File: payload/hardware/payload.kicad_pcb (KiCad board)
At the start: 4 copper layers, 80 x 80 mm, 43 parts, among them J10 Conn_02x20_Odd_Even, J2 ARJM11C7-502-AB, J3 USB_C_Receptacle_USB2.0_16P, J4 Conn_02x04_Odd_Even, J5 Conn_01x05, SW1 SW_Push, U1 CM4, U2 MCP2517FD-xJHA, U4 SN65HVD230, U5 MCP2517FD-xJHA, U6 74LVC1G07, U7 SN65HVD230, U9 DRV8846, Y1 20 MHz, Y2 20 MHz

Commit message: via spam, silk
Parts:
- added REF**: OSHW-Logo2_14.6x12mm_SilkScreen, Symbol:OSHW-Logo2_14.6x12mm_SilkScreen, B.Cu at (87.1, 129.1)
- SW1: footprint Button_Switch_SMD:SW_SPST_TS-1088-xR020 -> Button_Switch_SMD:SW_SPST_PTS810
- moved SW1 0.60 mm to (76.4, 82.2)
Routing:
- net /CM4/POWER_BUTTON: track 15.8 -> 21.4 mm
- net Net-(JP1-B): track 4.44 -> 7.82 mm
- net +5V: track 34.9 -> 31.6 mm, vias 1 -> 3
- net /CM4/ETH_P0-: track 28.5 -> 31.1 mm
- net /CM4/ETH_P2-: track 28.0 -> 30.5 mm
- net /CM4/ETH_P1+: track 25.9 -> 28.5 mm
- net /CM4/ETH_P3-: track 26.3 -> 27.9 mm
- net /CM4/Cameras/CAMERA_GPIO: track 102.4 -> 100.9 mm
- net /CM4/~{MOTOR_SLEEP}: track 61.1 -> 62.1 mm
- net Net-(J4-Pin_2): track 38.4 -> 39.1 mm
- net GND: vias 227 -> 536
- net +3V3: vias 15 -> 18
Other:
- board text added: "Ethan Eggbert frrt.space"
- board text added: "foo"

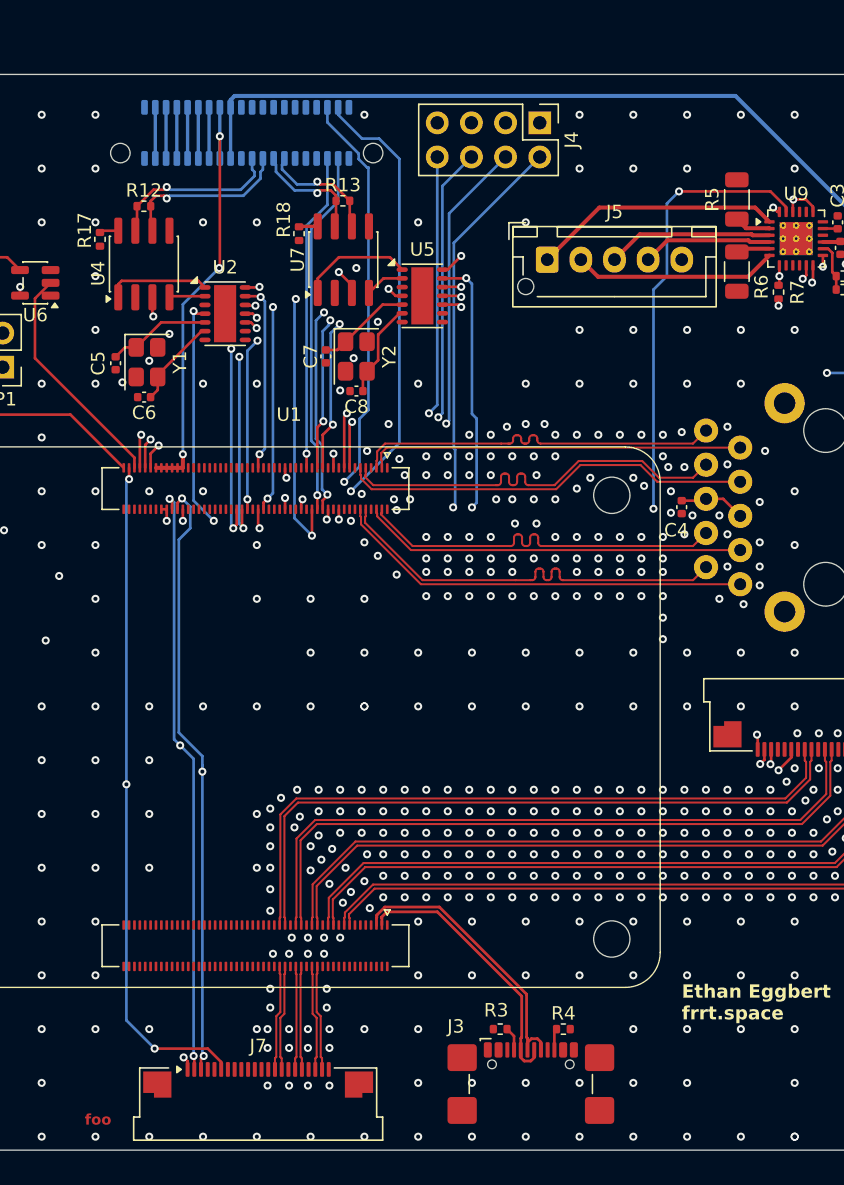
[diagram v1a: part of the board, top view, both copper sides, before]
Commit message: add decoupling caps, fix USB skew, add Jax's name
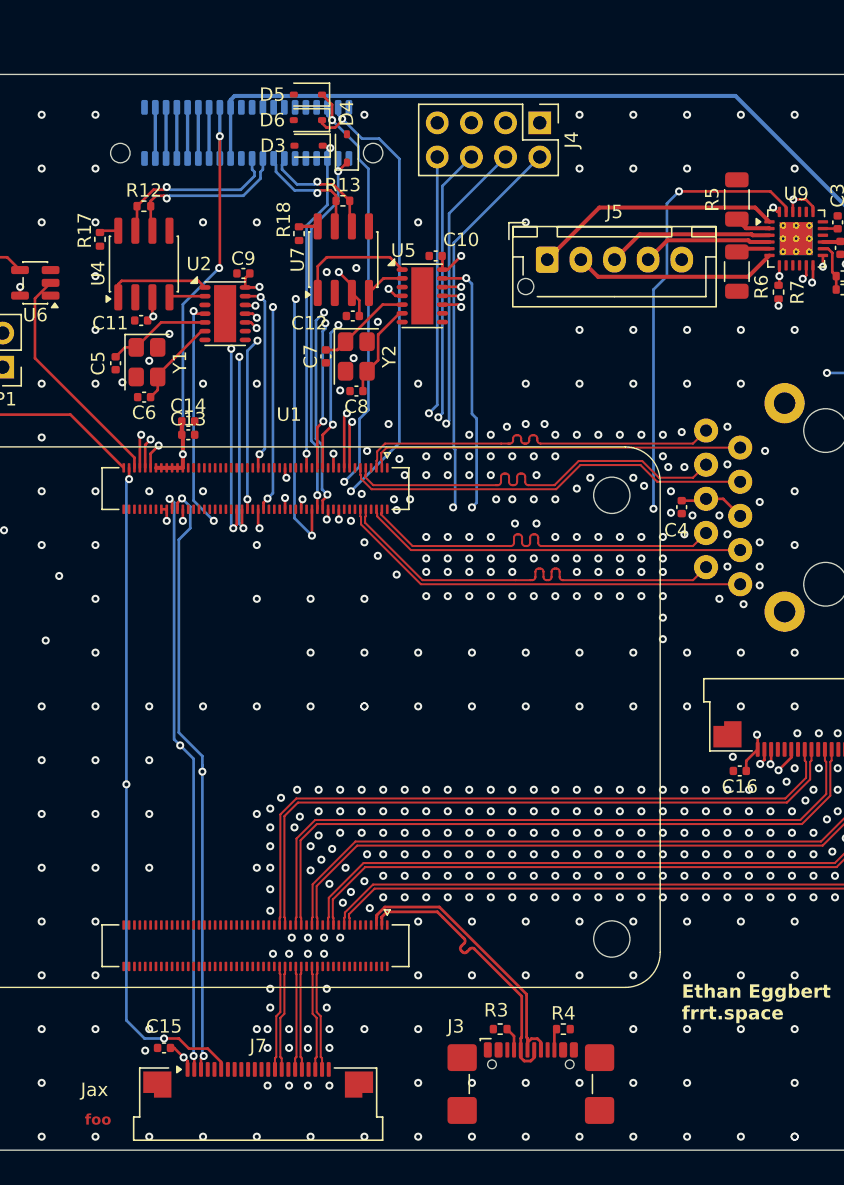
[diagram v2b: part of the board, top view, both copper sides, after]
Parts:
- removed REF**: OSHW-Logo2_14.6x12mm_SilkScreen, Symbol:OSHW-Logo2_14.6x12mm_SilkScreen
- added C10: 100n, Capacitor_SMD:C_0402_1005Metric, F.Cu at (113.3, 74.5)
- added C11: 100n, Capacitor_SMD:C_0402_1005Metric, F.Cu at (91.4, 79.3)
- added C12: 100n, Capacitor_SMD:C_0402_1005Metric, F.Cu at (107.1, 79.0)
- added C13: 100n, Capacitor_SMD:C_0402_1005Metric, F.Cu at (94.9, 87.8)
- added C14: 1u, Capacitor_SMD:C_0402_1005Metric, F.Cu at (94.9, 86.8)
- added C15: 100n, Capacitor_SMD:C_0402_1005Metric, F.Cu at (93.1, 133.4)
- added C16: 100n, Capacitor_SMD:C_0402_1005Metric, F.Cu at (135.9, 112.8)
- added C9: 100n, Capacitor_SMD:C_0402_1005Metric, F.Cu at (99.0, 75.8)
- added D3: D_Zener, Diode_SMD:D_SOD-323, F.Cu at (103.8, 66.3)
- added D4: D_Zener, Diode_SMD:D_SOD-323, F.Cu at (106.7, 66.5)
- added D5: D_Zener, Diode_SMD:D_SOD-323, F.Cu at (103.8, 62.5)
- added D6: D_Zener, Diode_SMD:D_SOD-323, F.Cu at (103.8, 64.4)
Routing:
- net +3V3: track 19.7 -> 27.6 mm
- net +5V: track 31.6 -> 34.1 mm
- net /CM4/UART1_RX: track 38.9 -> 41.1 mm, vias 2 -> 3
- net /CM4/UART1_TX: track 35.1 -> 37.3 mm, vias 2 -> 3
- net /CM4/UART2_TX: track 23.7 -> 25.2 mm, vias 1 -> 2
- net /CM4/USB_D-: track 20.2 -> 21.3 mm
- net /CM4/UART2_RX: track 27.1 -> 28.0 mm, vias 1 -> 2
- net MOSI: track 30.5 -> 29.9 mm
- net Net-(U5-TXCAN): track 8.40 -> 8.92 mm
- net GND: vias 536 -> 539
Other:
- board text added: "Jax"

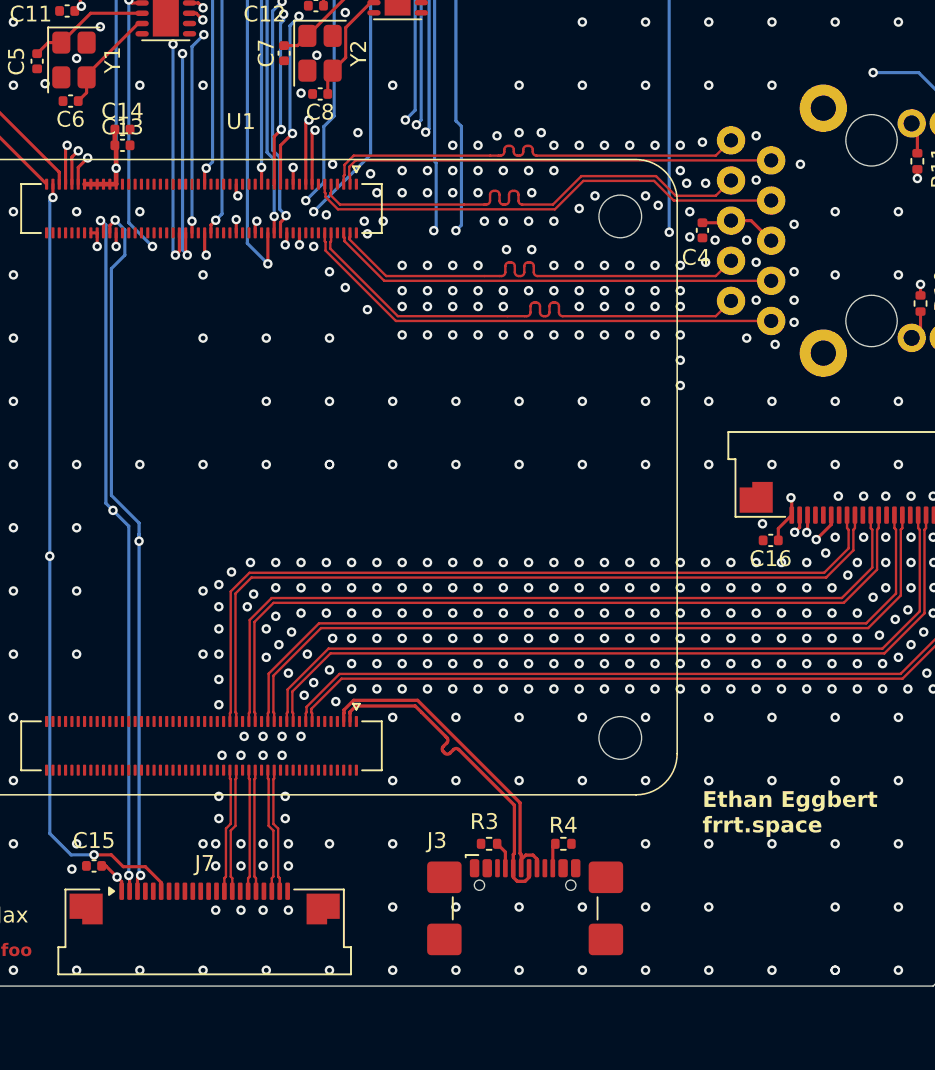
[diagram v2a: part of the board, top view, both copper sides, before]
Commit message: DRC fixes and add 3d models
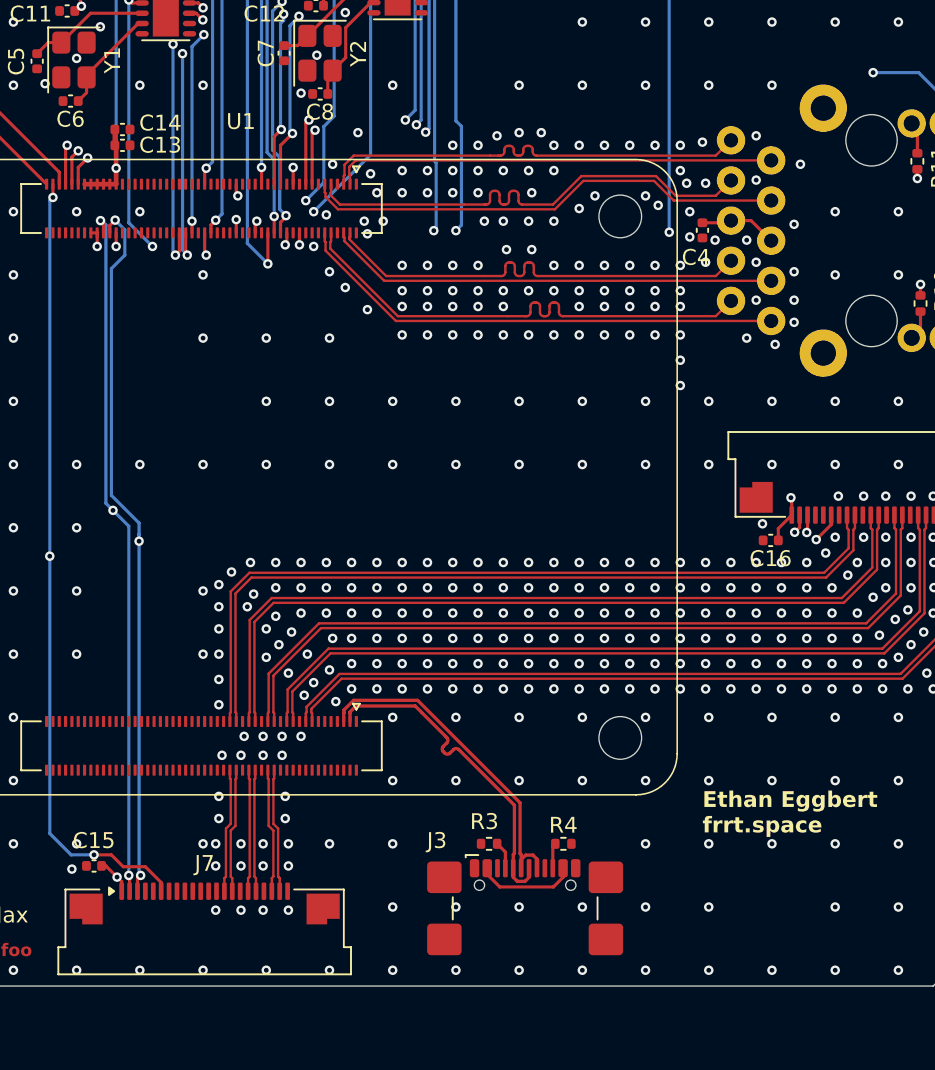
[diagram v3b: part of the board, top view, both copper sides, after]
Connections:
- J3 pad A4: unconnected-(J3-VBUS-PadA4)_3 -> Net-(J3-VBUS-PadA4)
- J3 pad A9: unconnected-(J3-VBUS-PadA4) -> Net-(J3-VBUS-PadA4)
- J3 pad B4: unconnected-(J3-VBUS-PadA4)_1 -> Net-(J3-VBUS-PadA4)
- J3 pad B9: unconnected-(J3-VBUS-PadA4)_2 -> Net-(J3-VBUS-PadA4)
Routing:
- net Net-(J3-VBUS-PadA4): track 0.00 -> 6.34 mm
- net GND: vias 539 -> 540
- net +3V3: vias 18 -> 15

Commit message: added through holes
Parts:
- added ?: , , F.Cu at (81.0, 68.3)
- added ?: , , F.Cu at (81.2, 135.1)
- added ?: , , F.Cu at (147.3, 133.8)
- added ?: , , F.Cu at (146.1, 67.2)
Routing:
- net GND: vias 540 -> 538
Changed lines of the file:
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@@
 		)
 	)
+	(footprint ""
+		(layer "F.Cu")
+		(at 80.95 68.3)
+		(property "Reference" ""
+			(at 0 0 0)
+			(layer "F.SilkS")
+			(effects
+				(font
+					(size 1.27 1.27)
+				)
+			)
+		)
+		(property "Value" ""
+			(at 0 0 0)
+			(layer "F.Fab")
+			(effects
+				(font
+					(size 1.27 1.27)
+				)
+			)
+		)
+		(property "Datasheet" ""
+			(at 0 0 0)
+			(layer "F.Fab")
+			(hide yes)
+			(effects
+				(font
+					(size 1.27 1.27)
+				)
+			)
+		)
+		(property "Description" ""
+			(at 0 0 0)
+			(layer "F.Fab")
+			(hide yes)
+			(effects
+				(font
+					(size 1.27 1.27)
+				)
+			)
+		)
+		(duplicate_pad_numbers_are_jumpers no)
+		(pad "" np_thru_hole circle
+			(at 0 0)
+			(size 3.2 3.2)
+			(drill 3.2)
+			(layers "*.Cu" "*.Mask")
+		)
+		(embedded_fonts no)
+	)
 	(footprint "Resistor_SMD:R_0402_1005Metric"
 		(layer "F.Cu")
@@
 		)
 	)
+	(footprint ""
+		(layer "F.Cu")
+		(at 81.15 135.1)
+		(property "Reference" ""
+			(at 0 0 0)
+			(layer "F.SilkS")
+			(effects
+				(font
+					(size 1.27 1.27)
+				)
+			)
+		)
+		(property "Value" ""
+			(at 0 0 0)
+			(layer "F.Fab")
+			(effects
+				(font
+					(size 1.27 1.27)
+				)
+			)
+		)
+		(property "Datasheet" ""
+			(at 0 0 0)
+			(layer "F.Fab")
+			(hide yes)
+			(effects
+				(font
+					(size 1.27 1.27)
+				)
+			)
+		)
+		(property "Description" ""
+			(at 0 0 0)
+			(layer "F.Fab")
+			(hide yes)
+			(effects
+				(font
+					(size 1.27 1.27)
+				)
+			)
+		)
+		(duplicate_pad_numbers_are_jumpers no)
+		(pad "" np_thru_hole circle
+			(at 0 0)
+			(size 3.2 3.2)
+			(drill 3.2)
+			(layers "*.Cu" "*.Mask")
+		)
+		(embedded_fonts no)
+	)
 	(footprint "Crystal:Crystal_SMD_SeikoEpson_TSX3225-4Pin_3.2x2.5mm"
 		(layer "F.Cu")
@@
 		)
 	)
+	(footprint ""
+		(layer "F.Cu")
+		(at 147.35 133.85)
+		(property "Reference" ""
+			(at 0 0 0)
+			(layer "F.SilkS")
+			(effects
+				(font
+					(size 1.27 1.27)
+				)
+			)
+		)
+		(property "Value" ""
+			(at 0 0 0)
+			(layer "F.Fab")
+			(effects
+				(font
+					(size 1.27 1.27)
+				)
+			)
+		)
+		(property "Datasheet" ""
+			(at 0 0 0)
+			(layer "F.Fab")
+			(hide yes)
+			(effects
+				(font
+					(size 1.27 1.27)
+				)
+			)
+		)
+		(property "Description" ""
+			(at 0 0 0)
+			(layer "F.Fab")
+			(hide yes)
+			(effects
+				(font
+					(size 1.27 1.27)
+				)
+			)
+		)
+		(duplicate_pad_numbers_are_jumpers no)
+		(pad "" np_thru_hole circle
+			(at 0 0)
+			(size 3.2 3.2)
+			(drill 3.2)
+			(layers "*.Cu" "*.Mask")
+		)
+		(embedded_fonts no)
+	)
 	(footprint "LED_SMD:LED_0805_2012Metric"
 		(layer "F.Cu")
@@
 		)
 	)
+	(footprint ""
+		(layer "F.Cu")
+		(at 146.05 67.15)
+		(property "Reference" ""
+			(at 0 0 0)
+			(layer "F.SilkS")
+			(effects
+				(font
+					(size 1.27 1.27)
+				)
+			)
+		)
+		(property "Value" ""
+			(at 0 0 0)
+			(layer "F.Fab")
+			(effects
+				(font
+					(size 1.27 1.27)
+				)
+			)
+		)
+		(property "Datasheet" ""
+			(at 0 0 0)
+			(layer "F.Fab")
+			(hide yes)
+			(effects
+				(font
+					(size 1.27 1.27)
+				)
+			)
+		)
+		(property "Description" ""
+			(at 0 0 0)
+			(layer "F.Fab")
+			(hide yes)
+			(effects
+				(font
+					(size 1.27 1.27)
+				)
+			)
+		)
+		(duplicate_pad_numbers_are_jumpers no)
+		(pad "" np_thru_hole circle
+			(at 0 0)
+			(size 3.2 3.2)
+			(drill 3.2)
+			(layers "*.Cu" "*.Mask")
+		)
+		(embedded_fonts no)
+	)
 	(footprint "Button_Switch_SMD:SW_SPST_PTS810"
 		(layer "F.Cu")
@@
 	)
 	(via
-		(at 148 132)
+		(at 148 131.75)
 		(size 0.6)
 		(drill 0.3)
@@
 	)
 	(via
-		(at 148 68)
+		(at 148.25 68)
 		(size 0.6)
 		(drill 0.3)
@@
 	)
 	(via
-		(at 80 68)
-		(size 0.6)
-		(drill 0.3)
-		(layers "F.Cu" "B.Cu")
-		(free yes)
-		(net "GND")
-	)
-	(via
 		(at 140 108)
 		(size 0.6)
@@
 	)
 	(via
-		(at 80 136)
-		(size 0.6)
-		(drill 0.3)
-		(layers "F.Cu" "B.Cu")
-		(free yes)
-		(net "GND")
-	)
-	(via
 		(at 120.8 94.4)
 		(size 0.6)
@@
 	)
 	(segment
+		(start 122.78 134.119999)
+		(end 122.78 133.545)
+		(width 0.2)
+		(layer "F.Cu")
+		(net "Net-(J3-VBUS-PadA4)")
+	)
+	(segment
+		(start 117.98 133.931698)
+		(end 118.778002 134.7297)
+		(width 0.2)
+		(layer "F.Cu")
+		(net "Net-(J3-VBUS-PadA4)")
+	)
+	(segment
+		(start 122.170299 134.7297)
+		(end 122.78 134.119999)
+		(width 0.2)
+		(layer "F.Cu")
+		(net "Net-(J3-VBUS-PadA4)")
+	)
+	(segment
+		(start 117.98 133.545)
+		(end 117.98 133.931698)
+		(width 0.2)
+		(layer "F.Cu")
+		(net "Net-(J3-VBUS-PadA4)")
+	)
+	(segment
+		(start 118.778002 134.7297)
+		(end 122.170299 134.7297)
+		(width 0.2)
+		(layer "F.Cu")
+		(net "Net-(J3-VBUS-PadA4)")
+	)
+	(segment
 		(start 120.05985 129.405504)
 		(end 120.05985 132.612349)
@@
 		(net "/Inter Board Connector/RAIL_6_VOUT")
 	)
-	(segment
-		(start 122.78 134.119999)
-		(end 122.78 133.545)
-		(width 0.2)
-		(layer "F.Cu")
-		(net "Net-(J3-VBUS-PadA4)")
-	)
-	(segment
-		(start 117.98 133.931698)
-		(end 118.778002 134.7297)
-		(width 0.2)
-		(layer "F.Cu")
-		(net "Net-(J3-VBUS-PadA4)")
-	)
-	(segment
-		(start 122.170299 134.7297)
-		(end 122.78 134.119999)
-		(width 0.2)
-		(layer "F.Cu")
-		(net "Net-(J3-VBUS-PadA4)")
-	)
-	(segment
-		(start 117.98 133.545)
-		(end 117.98 133.931698)
-		(width 0.2)
-		(layer "F.Cu")
-		(net "Net-(J3-VBUS-PadA4)")
-	)
-	(segment
-		(start 118.778002 134.7297)
-		(end 122.170299 134.7297)
-		(width 0.2)
-		(layer "F.Cu")
-		(net "Net-(J3-VBUS-PadA4)")
-	)
 	(zone

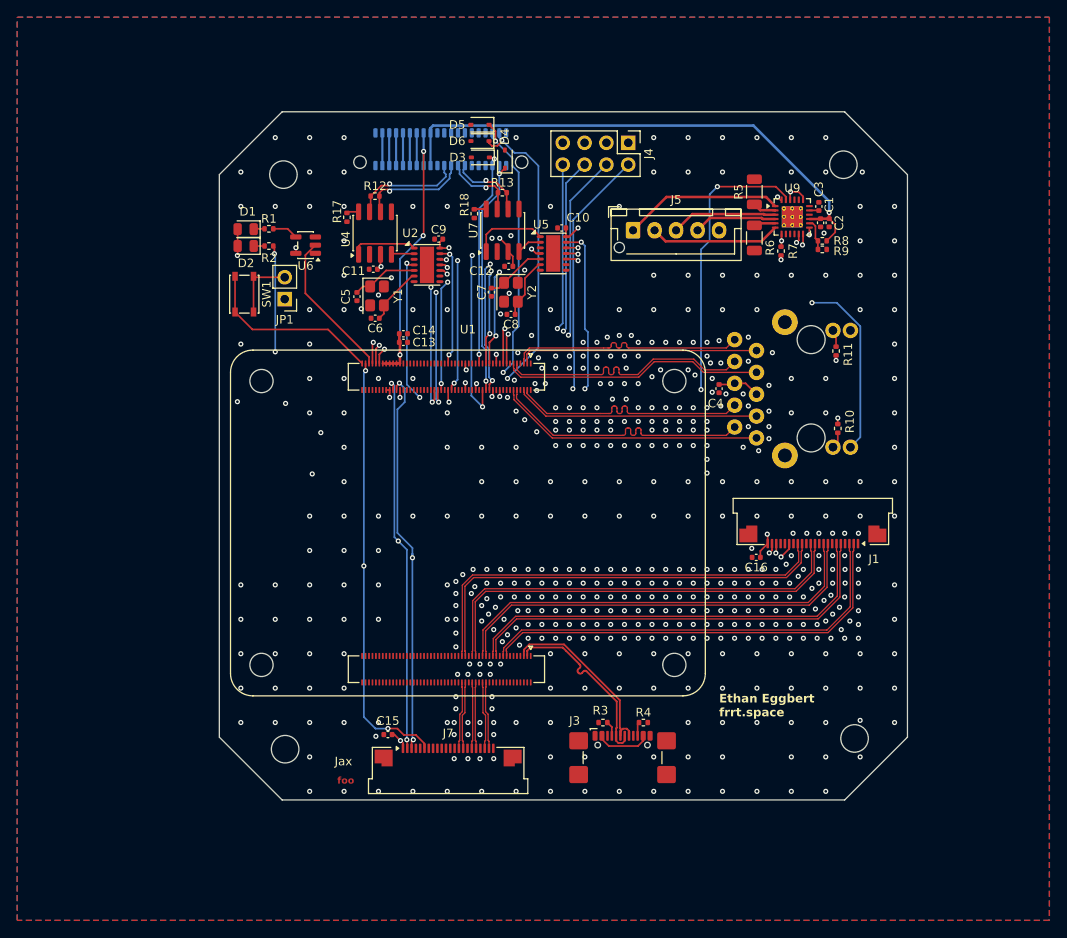
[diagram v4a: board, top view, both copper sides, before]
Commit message: mounting holes
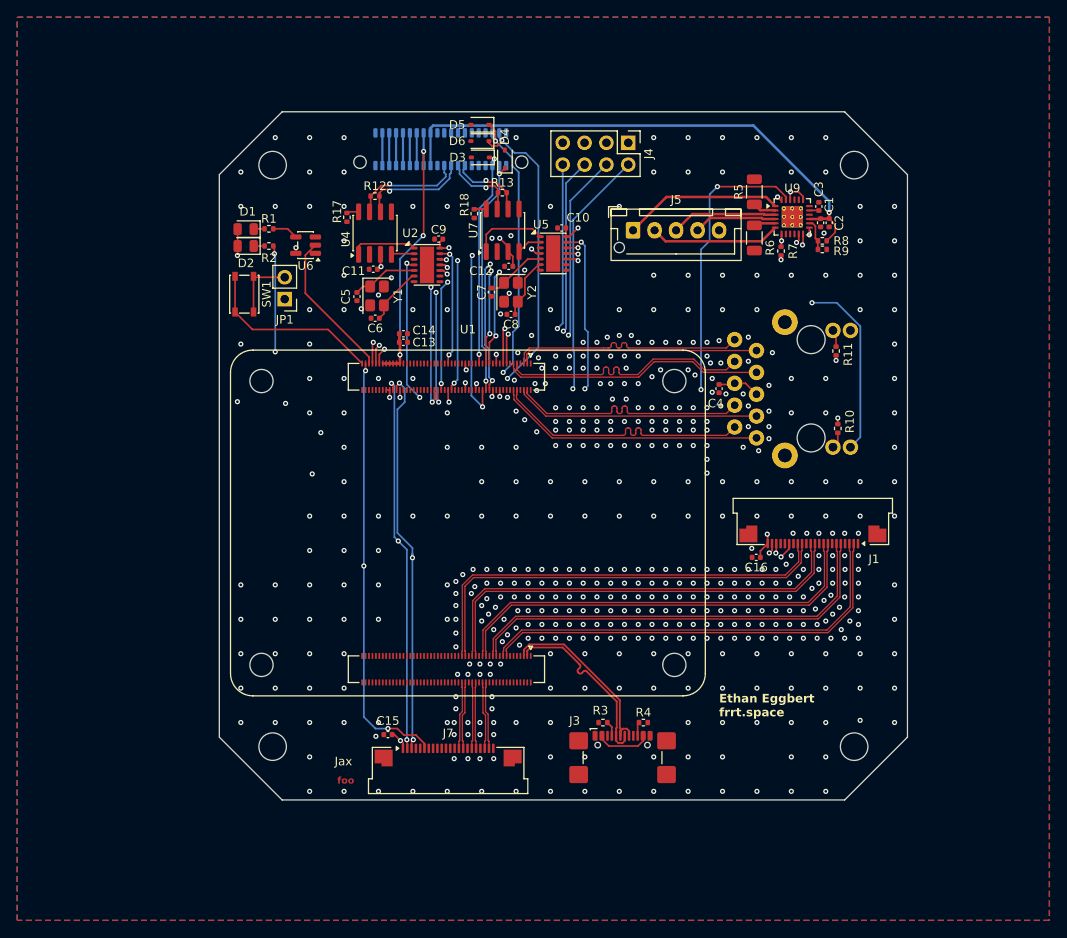
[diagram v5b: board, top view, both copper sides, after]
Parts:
- moved ? 1.67 mm to (79.7, 67.2)
- moved ? 1.48 mm to (79.7, 134.8)
- moved ? 1.25 mm to (147.3, 67.2)
- moved ? 0.96 mm to (147.3, 134.8)
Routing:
- net GND: vias 538 -> 536
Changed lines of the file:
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@@
 	(footprint ""
 		(layer "F.Cu")
-		(at 80.95 68.3)
+		(at 79.696 67.196)
 		(property "Reference" ""
 			(at 0 0 0)
@@
 	(footprint ""
 		(layer "F.Cu")
-		(at 81.15 135.1)
+		(at 79.696 134.804)
 		(property "Reference" ""
 			(at 0 0 0)
@@
 	(footprint ""
 		(layer "F.Cu")
-		(at 147.35 133.85)
+		(at 147.304 134.804)
 		(property "Reference" ""
 			(at 0 0 0)
@@
 	(footprint ""
 		(layer "F.Cu")
-		(at 146.05 67.15)
+		(at 147.304 67.196)
 		(property "Reference" ""
 			(at 0 0 0)
@@
 	)
 	(via
-		(at 148.25 68)
-		(size 0.6)
-		(drill 0.3)
-		(layers "F.Cu" "B.Cu")
-		(free yes)
-		(net "GND")
-	)
-	(via
 		(at 132 84)
 		(size 0.6)
@@
 		(size 0.6)
 		(drill 0.3)
-		(layers "F.Cu" "B.Cu")
-		(free yes)
-		(net "GND")
-	)
-	(via
-		(at 148 136)
-		(size 0.6)
-		(drill 0.3)

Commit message: add extra grounding vias, open source hardware silk, and make release
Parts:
- added REF**: OSHW-Logo2_14.6x12mm_SilkScreen, Symbol:OSHW-Logo2_14.6x12mm_SilkScreen, B.Cu at (110.8, 106.6)
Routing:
- net GND: vias 536 -> 544
